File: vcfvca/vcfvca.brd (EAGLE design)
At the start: 160 x 50.5 mm, 104 parts, among them IC1 LM13700N, IC2 LM4558N, IC3 LM13700N, IC4 LM13700N, IC5 LM4558N, J1 POWER, J2 FREQ, J3 RES, J4 AMP, J5 AUD_IN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

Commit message: Minor fixes
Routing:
- net -15V: track 292.0 -> 288.4 mm
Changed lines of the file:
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@@
 <wire x1="20.583025" y1="25.4" x2="24.13" y2="25.4" width="0.8128" layer="1"/>
 <wire x1="74.82105" y1="37.99105" x2="76.617103125" y2="38.735" width="0.8128" layer="1" curve="-45"/>
-<wire x1="85.942896875" y1="38.735" x2="87.73895" y2="37.99105" width="0.8128" layer="1" curve="-45"/>
-<wire x1="87.73895" y1="37.99105" x2="88.265" y2="37.465" width="0.8128" layer="1"/>
-<wire x1="89.798025" y1="36.83" x2="88.265" y2="37.465" width="0.8128" layer="1" curve="-45"/>
 <wire x1="102.34395" y1="36.08605" x2="100.547896875" y2="36.83" width="0.8128" layer="1" curve="45"/>
 <wire x1="102.34395" y1="36.08605" x2="104.14" y2="34.29" width="0.8128" layer="1"/>
@@
 <wire x1="71.12" y1="34.29" x2="74.82105" y2="37.99105" width="1.2192" layer="1"/>
 <wire x1="74.82105" y1="37.99105" x2="76.617103125" y2="38.735" width="1.2192" layer="1" curve="-45"/>
-<wire x1="76.617103125" y1="38.735" x2="85.942896875" y2="38.735" width="1.2192" layer="1"/>
-<wire x1="85.942896875" y1="38.735" x2="87.73895" y2="37.99105" width="1.2192" layer="1" curve="-45"/>
-<wire x1="88.265" y1="37.465" x2="89.798025" y2="36.83" width="1.2192" layer="1" curve="45"/>
-<wire x1="89.798025" y1="36.83" x2="100.547896875" y2="36.83" width="1.2192" layer="1"/>
+<wire x1="76.617103125" y1="38.735" x2="88.382975" y2="38.735" width="1.2192" layer="1"/>
+<wire x1="92.238103125" y1="36.83" x2="100.547896875" y2="36.83" width="1.2192" layer="1"/>
 <wire x1="100.547896875" y1="36.83" x2="109.22" y2="36.83" width="1.2192" layer="1"/>
 <wire x1="11.049" y1="21.59" x2="11.049" y2="24.093896875" width="1.2192" layer="1"/>
@@
 <wire x1="10.30505" y1="25.88995" x2="10.16" y2="26.035" width="1.2192" layer="1"/>
 <wire x1="9.86255" y1="26.33245" x2="8.066496875" y2="27.0764" width="1.2192" layer="1" curve="45"/>
+<wire x1="88.382975" y1="38.735" x2="89.916" y2="38.1" width="1.2192" layer="1" curve="-45"/>
+<wire x1="89.916" y1="38.1" x2="90.44205" y2="37.57395" width="1.2192" layer="1"/>
+<wire x1="90.44205" y1="37.57395" x2="92.238103125" y2="36.83" width="1.2192" layer="1" curve="45"/>
 </signal>
 <signal name="N$2">
@@
 <contactref element="R24" pad="1"/>
 <contactref element="IC3" pad="13"/>
-<wire x1="78.74" y1="35.56" x2="76.2" y2="35.56" width="0.4064" layer="16"/>
-<wire x1="74.93" y1="34.29" x2="76.2" y2="35.56" width="0.4064" layer="16"/>
-<wire x1="78.74" y1="35.56" x2="80.164078125" y2="35.56" width="0.4064" layer="16"/>
-<wire x1="80.164078125" y1="35.56" x2="81.697103125" y2="36.195" width="0.4064" layer="16" curve="45"/>
 <wire x1="95.25" y1="30.48" x2="94.8009875" y2="31.5640125" width="0.4064" layer="16" curve="45"/>
 <wire x1="93.7940125" y1="32.5709875" x2="92.71" y2="33.02" width="0.4064" layer="16" curve="45"/>
@@
 <wire x1="90.17" y1="34.29" x2="89.00895" y2="35.45105" width="0.4064" layer="16"/>
 <wire x1="89.00895" y1="35.45105" x2="87.212896875" y2="36.195" width="0.4064" layer="16" curve="45"/>
-<wire x1="87.212896875" y1="36.195" x2="81.697103125" y2="36.195" width="0.4064" layer="16"/>
+<wire x1="87.212896875" y1="36.195" x2="82.042" y2="36.195" width="0.4064" layer="16"/>
+<wire x1="82.042" y1="36.195" x2="81.697103125" y2="36.195" width="0.4064" layer="16"/>
+<wire x1="74.93" y1="34.29" x2="75.45605" y2="34.81605" width="0.4064" layer="16"/>
+<wire x1="75.45605" y1="34.81605" x2="77.252103125" y2="35.56" width="0.4064" layer="16" curve="-45"/>
+<wire x1="77.252103125" y1="35.56" x2="78.74" y2="35.56" width="0.4064" layer="16"/>
+<wire x1="78.74" y1="35.56" x2="79.650790625" y2="35.56" width="0.4064" layer="16"/>
+<wire x1="79.650790625" y1="35.56" x2="80.264" y2="35.814" width="0.4064" layer="16" curve="45"/>
+<wire x1="80.264" y1="35.814" x2="81.183815625" y2="36.195" width="0.4064" layer="16" curve="-45"/>
+<wire x1="81.183815625" y1="36.195" x2="81.697103125" y2="36.195" width="0.4064" layer="16"/>
 </signal>
 <signal name="N$21">

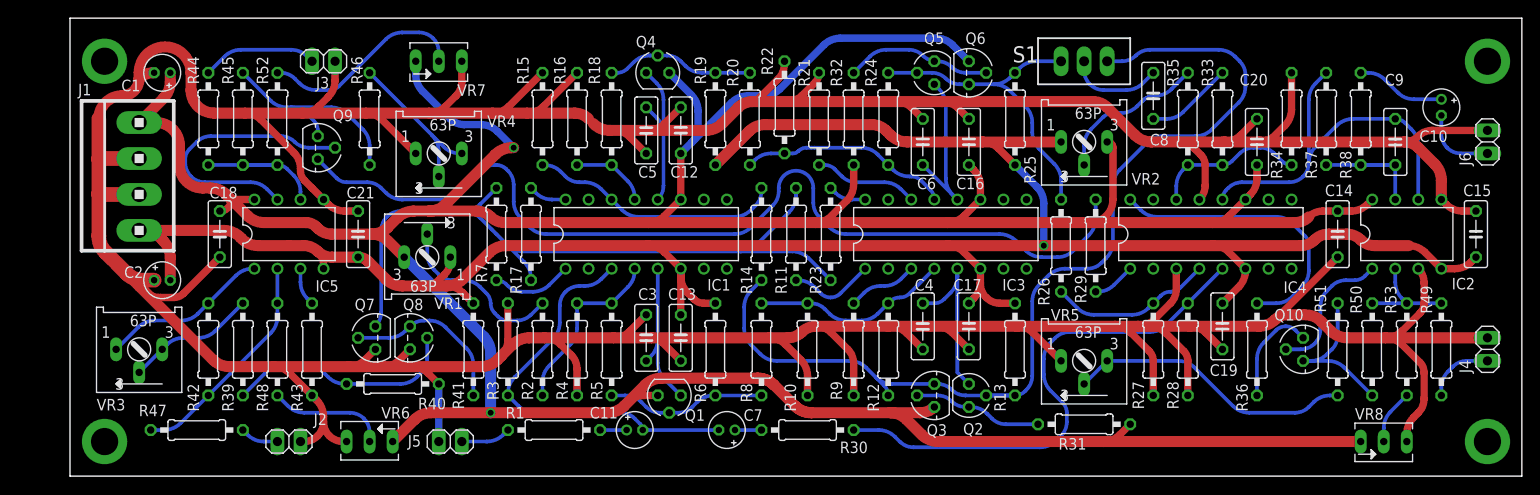
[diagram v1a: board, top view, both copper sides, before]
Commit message: Add ferrite bead, reroute
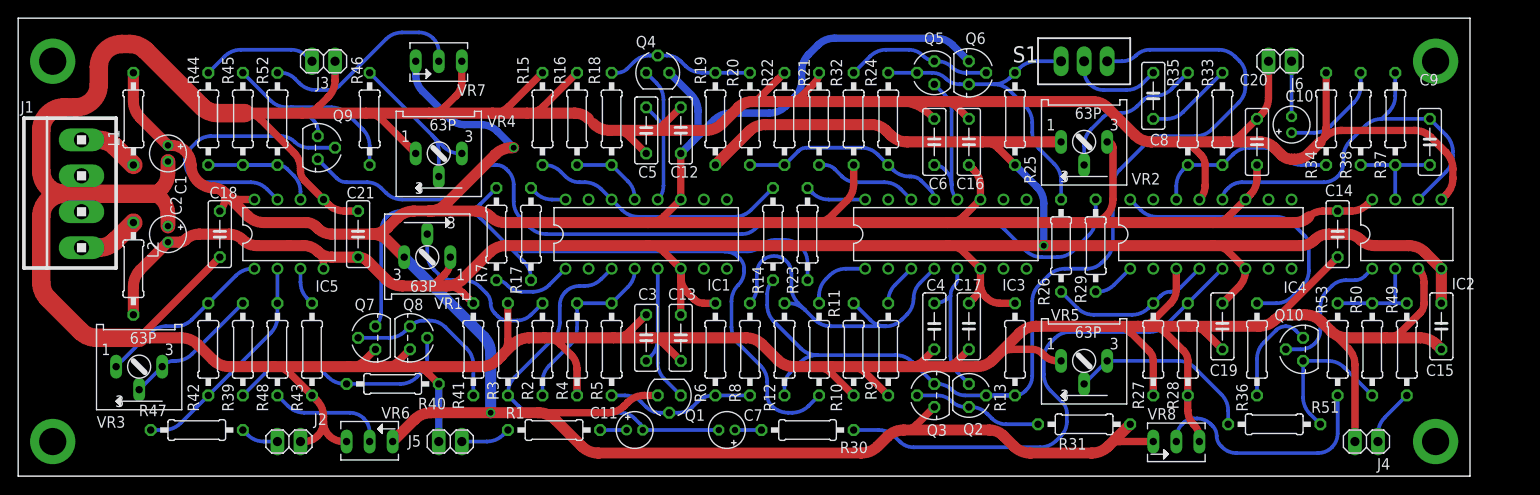
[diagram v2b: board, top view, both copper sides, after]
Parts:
- added L1, L2: FB, rcl:0207/10
- moved J6 24.5 mm to (133.3, 45.7), turned to 180 degrees
- moved VR8 22.9 mm to (121.9, 3.81)
- moved J4 16.8 mm to (142.9, 3.81), turned to 180 degrees
- moved C10 16.6 mm to (134.6, 38.7), turned to 90 degrees
- moved R11 13.0 mm to (82.5, 14.0), turned to 270 degrees
- moved R12 11.4 mm to (78.7, 14.0)
- moved C15 10.9 mm to (151.1, 16.5), turned to 90 degrees
- moved R51 10.8 mm to (132.7, 5.71), turned to 180 degrees
- moved C1 8.91 mm to (10.8, 35.6), turned to 270 degrees
- moved R37 7.62 mm to (146.1, 39.4)
- moved R53 7.62 mm to (139.7, 14.0)
- moved J1 6.63 mm to (1.27, 31.1)
- moved C2 5.12 mm to (10.8, 26.7), turned to 270 degrees
- moved R10 5.08 mm to (86.4, 14.0)
- moved C9 3.81 mm to (149.9, 36.8)
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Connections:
- new net N$63: J1.1, L1.1
- new net N$64: J1.4, L2.1
- net +15V: now also L1.2; no longer J1.1
- net -15V: now also L2.2; no longer J1.4
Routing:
- net +15V: track 439.2 -> 412.9 mm
- net N$60: track 5.97 -> 26.5 mm
- net I_FREQ: track 83.2 -> 98.8 mm
- net N$12: track 21.6 -> 36.8 mm
- net GND: track 671.8 -> 686.0 mm
- net -15V: track 288.4 -> 275.0 mm
- net N$45: track 31.5 -> 21.0 mm
- net N$64: track 0.00 -> 6.70 mm
- net N$63: track 0.00 -> 6.70 mm
- net I_RES: track 104.0 -> 98.9 mm
- net N$2: track 19.5 -> 15.5 mm
- net N$30: track 16.7 -> 20.5 mm
- net N$35: track 15.2 -> 11.4 mm
- net N$11: track 7.61 -> 4.70 mm
- net N$24: track 4.18 -> 6.72 mm
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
